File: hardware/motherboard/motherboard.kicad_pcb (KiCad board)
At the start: 4 copper layers, 152 x 68 mm, 82 parts, among them J1 IMU Connector, J2 JST-VH, J3 JST-VH, J4 JST-PH, J5 USB C 2.0, Q1 TSM7P06CP_ROG, Q2 TSM7P06CP_ROG, SW1 A, SW10 Right, SW11 Left, SW12 Up, SW13 Reset, SW2 B, SW3 X, SW4 Y, SW5 LB, SW6 RB, SW7 Start, SW8 Select, SW9 Down, U1 ESP32-S3-WROOM-1, U2 MCP73831-2-OT, U3 TPS75533KTTRG3, U4 TLV75709PDBV, U5 COM-09032

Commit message: Labelled Test Points
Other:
- board text added: "3V3"
- board text added: "Abat"
- board text added: "GND"
- board text added: "VBat"
- board text added: "VIN"
- board text added: "Vperipheral"
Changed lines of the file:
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@@
 		(layer "Edge.Cuts")
+	)
+	(gr_text "Vperipheral"
+		(at 80.01 40.64 0)
+		(layer "B.SilkS")
+		(effects
+			(font
+				(size 1 1)
+				(thickness 0.17)
+				(bold yes)
+			)
+			(justify left bottom mirror)
+		)
+	)
+	(gr_text "VBat"
+		(at 78.105 33.02 0)
+		(layer "B.SilkS")
+		(effects
+			(font
+				(size 1 1)
+				(thickness 0.17)
+				(bold yes)
+			)
+			(justify left bottom mirror)
+		)
+	)
+	(gr_text "3V3"
+		(at 103.505 28.575 0)
+		(layer "B.SilkS")
+		(effects
+			(font
+				(size 1 1)
+				(thickness 0.17)
+				(bold yes)
+			)
+			(justify left bottom mirror)
+		)
+	)
+	(gr_text "VIN"
+		(at 48.26 21.59 0)
+		(layer "B.SilkS")
+		(effects
+			(font
+				(size 1 1)
+				(thickness 0.17)
+				(bold yes)
+			)
+			(justify left bottom mirror)
+		)
+	)
+	(gr_text "GND"
+		(at 63.5 40.64 0)
+		(layer "B.SilkS")
+		(effects
+			(font
+				(size 1 1)
+				(thickness 0.17)
+				(bold yes)
+			)
+			(justify left bottom mirror)
+		)
+	)
+	(gr_text "Abat"
+		(at 82.55 33.02 0)
+		(layer "B.SilkS")
+		(effects
+			(font
+				(size 1 1)
+				(thickness 0.17)
+				(bold yes)
+			)
+			(justify left bottom mirror)
+		)
 	)
 	(gr_text "Battery"

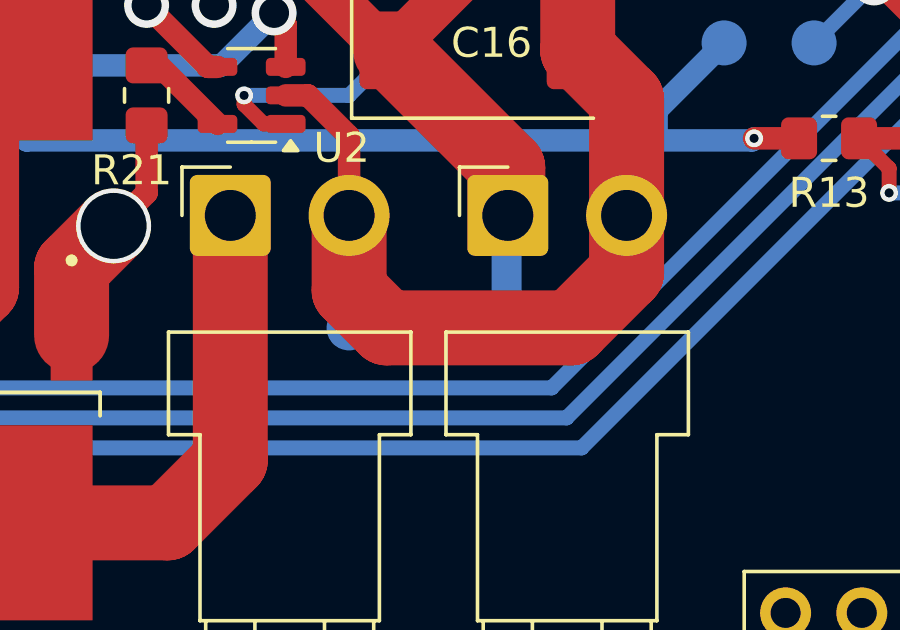
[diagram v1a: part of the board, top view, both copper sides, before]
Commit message: Labelled power connectors on Motherboard
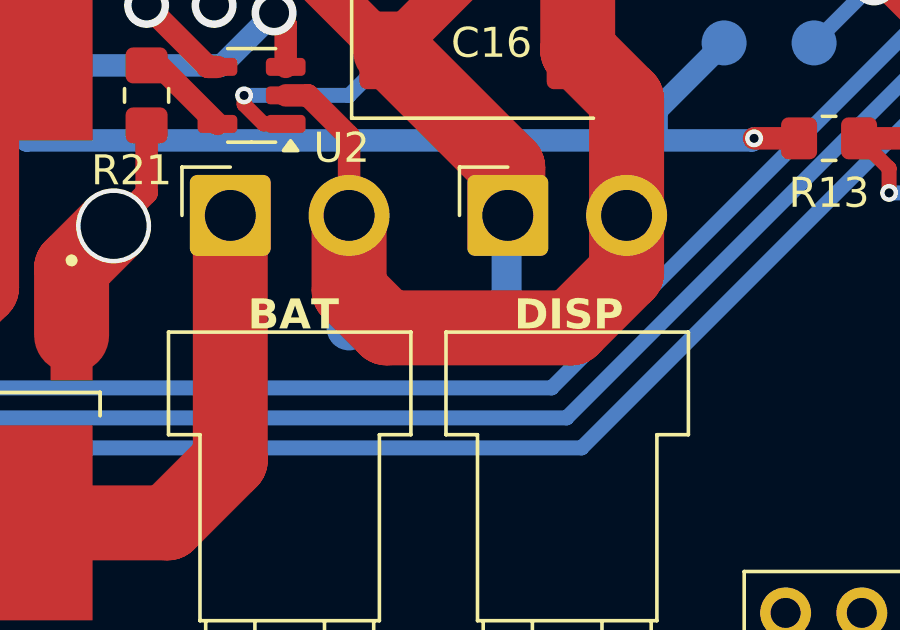
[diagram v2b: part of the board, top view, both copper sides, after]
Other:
- board text added: "BAT"
- board text added: "DISP"
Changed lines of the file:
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@@
 		(layer "Edge.Cuts")
+	)
+	(gr_text "BAT"
+		(at 61.372916 40.14 0)
+		(layer "F.SilkS")
+		(effects
+			(font
+				(size 1 1)
+				(thickness 0.17)
+				(bold yes)
+			)
+			(justify left bottom)
+		)
+	)
+	(gr_text "DISP"
+		(at 70.254377 40.14 0)
+		(layer "F.SilkS")
+		(effects
+			(font
+				(size 1 1)
+				(thickness 0.17)
+				(bold yes)
+			)
+			(justify left bottom)
+		)
 	)
 	(gr_text "Vperipheral"

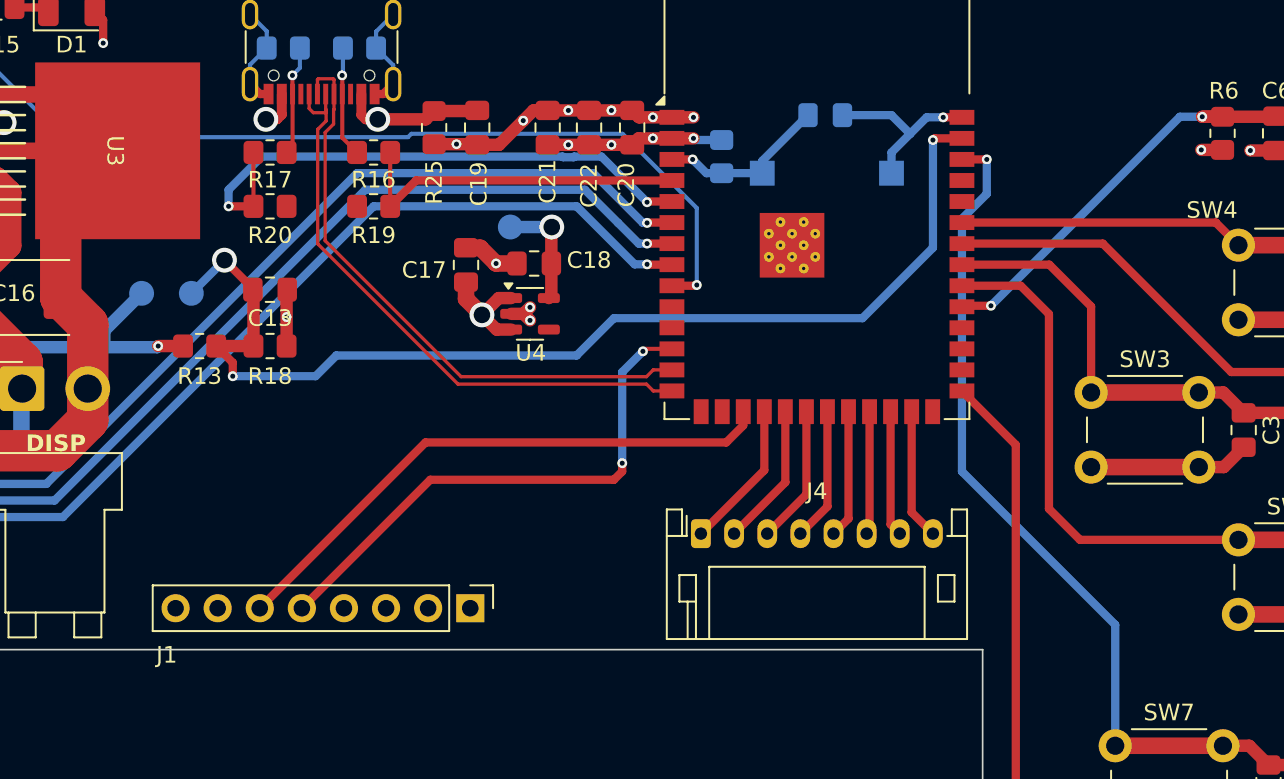
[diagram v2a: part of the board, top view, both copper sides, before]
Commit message: Updated Schematic, Added motor/speaker connector
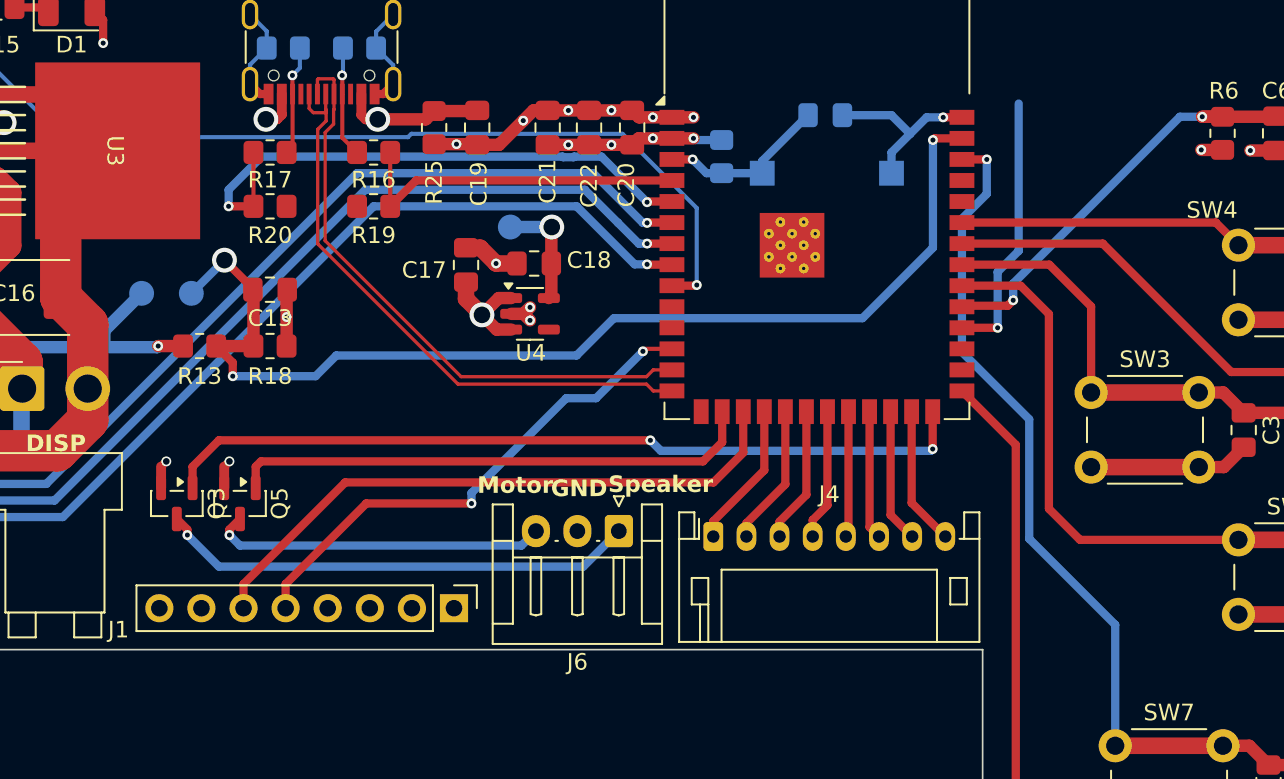
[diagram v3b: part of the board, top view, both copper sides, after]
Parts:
- added J6: Conn_01x03_Pin, Connector_JST:JST_EH_S3B-EH_1x03_P2.50mm_Horizontal, F.Cu at (106.0, 44.8)
- added Q3: AO3400A, Package_TO_SOT_SMD:SOT-23, F.Cu at (79.4, 43.2)
- added Q5: AO3400A, Package_TO_SOT_SMD:SOT-23, F.Cu at (83.2, 43.2)
- moved J1 0.98 mm to (87.6, 58.0)
- moved J4 0.77 mm to (111.7, 45.2)
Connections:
- U1 pad 16: unconnected-(U1-IO46-Pad16) -> Motor
- U1 pad 26: unconnected-(U1-IO45-Pad26) -> Speaker
- U1 pad 28: unconnected-(U1-IO35-Pad28) -> Left
- U1 pad 29: unconnected-(U1-IO36-Pad29) -> Down
- U1 pad 30: unconnected-(U1-IO37-Pad30) -> BLeft
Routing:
- net Speaker: track 0.00 -> 49.2 mm, vias 0 -> 2
- net Motor: track 0.00 -> 31.9 mm
- net Net-(J6-Pin_1): track 0.00 -> 28.9 mm, vias 0 -> 1
- net Net-(J6-Pin_3): track 0.00 -> 20.3 mm, vias 0 -> 1
- net VPeripheral: track 36.3 -> 55.3 mm, vias 0 -> 2
- net BLeft: track 7.76 -> 24.0 mm, vias 0 -> 1
- net SCL: track 34.6 -> 37.4 mm
- net SDA: track 32.3 -> 31.0 mm
- net BRight: track 28.7 -> 29.3 mm
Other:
- board text added: "Motor"
- board text added: "Speaker"

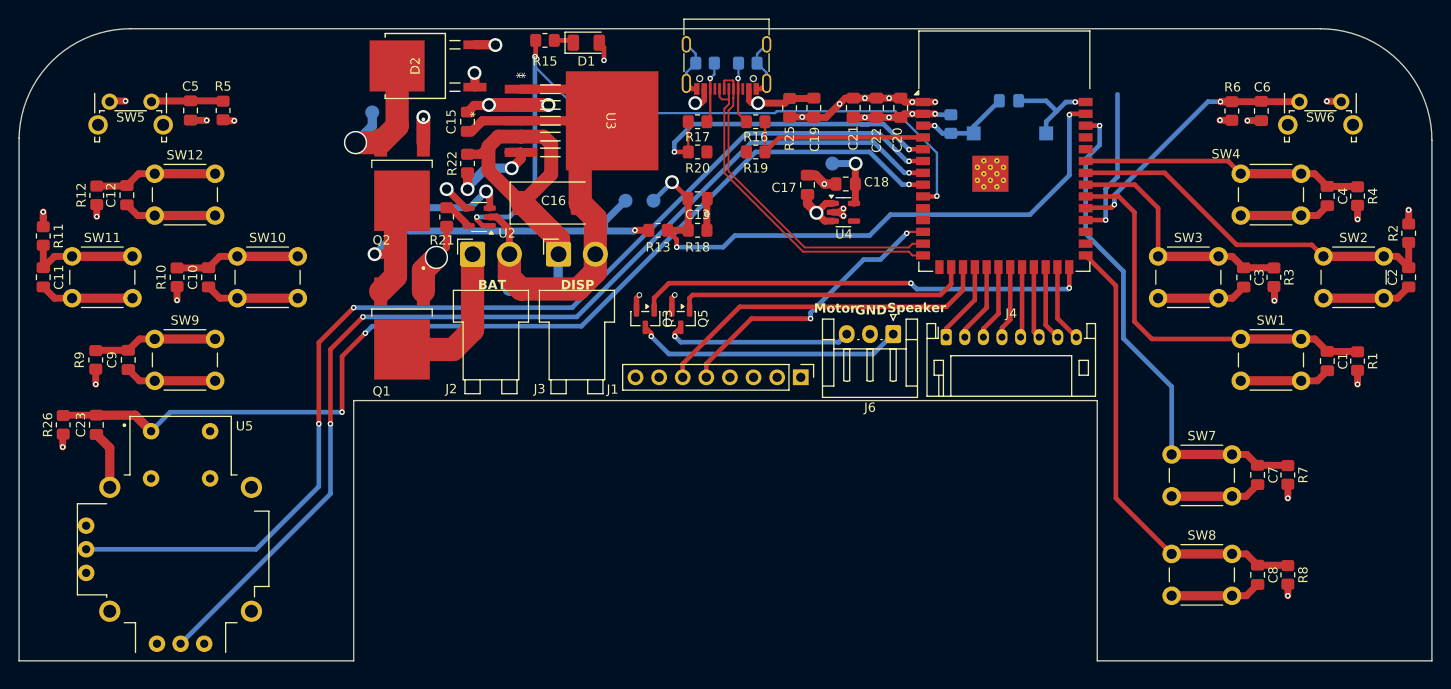
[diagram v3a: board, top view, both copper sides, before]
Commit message: Added ucbc 3d model
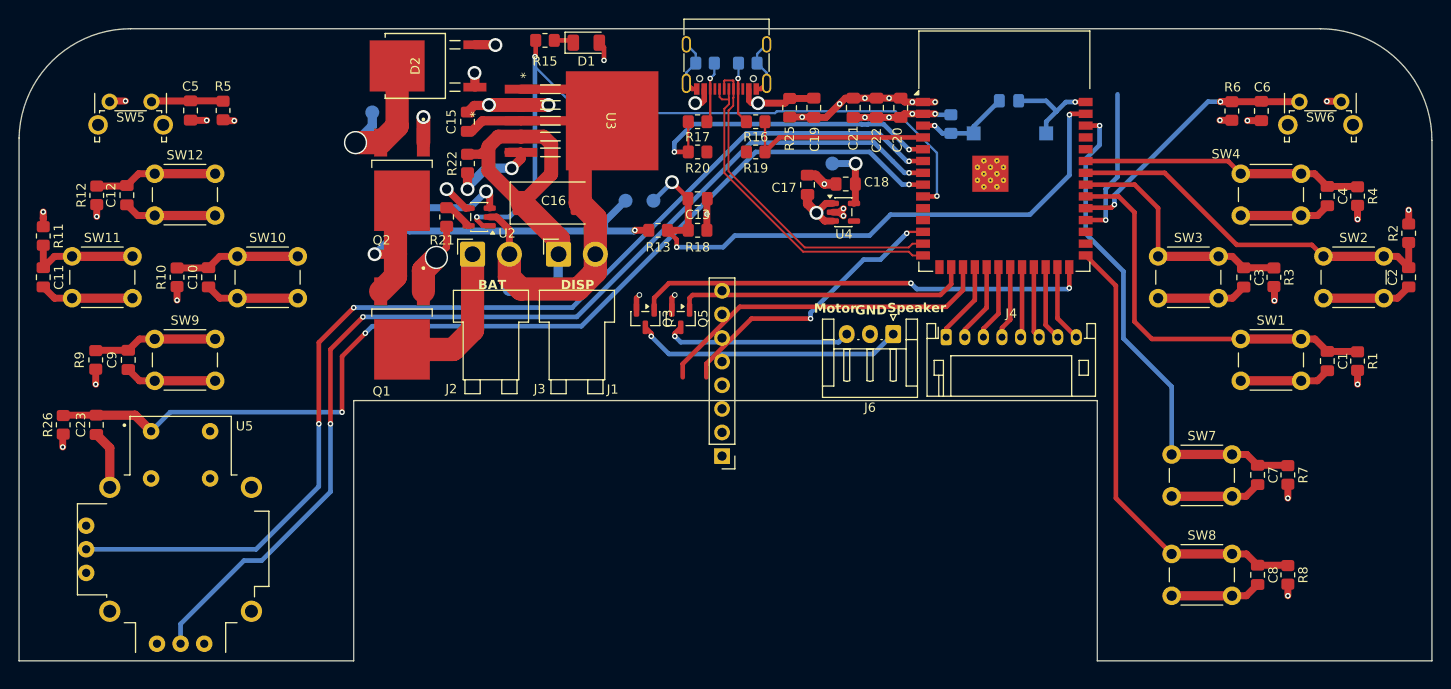
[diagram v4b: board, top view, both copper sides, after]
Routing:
- net AX: track 112.6 -> 113.8 mm
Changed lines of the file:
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@@
 			(pinfunction "Pin_2")
 			(pintype "passive")
-			(thermal_bridge_width 1)
 		)
 		(embedded_fonts no)
@@
 			(polygon
 				(pts
-					(xy 94 18.39) (xy 142.030402 18.474403) (xy 141.971359 -2.61) (xy 94 -2.61)
+					(xy 94 18.39) (xy 142 18.39) (xy 142 -2.61) (xy 94 -2.61)
 				)
 			)
@@
 		(attr smd)
 		(fp_line
-			(start 0 -1.56)
-			(end -0.8 -1.56)
+			(start -0.91 -1.56)
+			(end 0.91 -1.56)
 			(stroke
 				(width 0.12)
@@
 		)
 		(fp_line
-			(start 0 -1.56)
-			(end 0.8 -1.56)
+			(start -0.91 -1.51)
+			(end -0.91 -1.56)
 			(stroke
 				(width 0.12)
@@
 		)
 		(fp_line
-			(start 0 1.56)
-			(end -0.8 1.56)
+			(start -0.91 1.56)
+			(end -0.91 1.51)
 			(stroke
 				(width 0.12)
@@
 		)
 		(fp_line
-			(start 0 1.56)
-			(end 0.8 1.56)
+			(start 0.91 -1.56)
+			(end 0.91 -1.51)
+			(stroke
+				(width 0.12)
+				(type solid)
+			)
+			(layer "F.SilkS")
+		)
+		(fp_line
+			(start 0.91 -0.39)
+			(end 0.91 0.39)
+			(stroke
+				(width 0.12)
+				(type solid)
+			)
+			(layer "F.SilkS")
+		)
+		(fp_line
+			(start 0.91 1.51)
+			(end 0.91 1.56)
+			(stroke
+				(width 0.12)
+				(type solid)
+			)
+			(layer "F.SilkS")
+		)
+		(fp_line
+			(start 0.91 1.56)
+			(end -0.91 1.56)
 			(stroke
 				(width 0.12)
@@
 		(fp_poly
 			(pts
-				(xy -1.3 -1.51) (xy -1.54 -1.84) (xy -1.06 -1.84)
+				(xy -1.45 -1.51) (xy -1.69 -1.84) (xy -1.21 -1.84)
 			)
 			(stroke
@@
 		)
 		(embedded_fonts no)
-		(model "${KICAD9_3DMODEL_DIR}/Connector_USB.3dshapes/USB_C_Receptacle_G-Switch_GT-USB-7010ASV.step"
+		(model "${OPS2_HANDHELD}/esp_32_handheld.3dshapes/664_12402012E212A.stp"
 			(offset
-				(xyz 0 0 0)
+				(xyz 40 1 1.5)
 			)
 			(scale
@@
 			)
 			(rotate
-				(xyz 0 0 0)
+				(xyz -90 -0 -0)
 			)
 		)
@@
 		)
 		(fp_text user "*"
-			(at -4.884999 9.652 90)
+			(at -4.884999 9.652 270)
+			(unlocked yes)
 			(layer "F.SilkS")
 			(effects
@@
 		)
 		(fp_text user "*"
-			(at -4.884999 9.652 90)
+			(at -4.884999 9.652 270)
+			(unlocked yes)
 			(layer "F.Fab")
 			(effects
@@
 			(pinfunction "Pin_2")
 			(pintype "passive")
-			(thermal_bridge_width 1)
 		)
 		(embedded_fonts no)
@@
 		(fp_text user "*"
 			(at -5.195001 6.4135 90)
-			(unlocked yes)
 			(layer "F.SilkS")
 			(effects
@@
 		(attr smd)
 		(fp_line
-			(start 0 1.56)
-			(end 0.8 1.56)
+			(start 0.91 1.56)
+			(end -0.91 1.56)
+			(stroke
+				(width 0.12)
+				(type solid)
+			)
+			(layer "F.SilkS")
+		)
+		(fp_line
+			(start 0.91 1.51)
+			(end 0.91 1.56)
+			(stroke
+				(width 0.12)
+				(type solid)
+			)
+			(layer "F.SilkS")
+		)
+		(fp_line
+			(start 0.91 -0.39)
+			(end 0.91 0.39)
+			(stroke
+				(width 0.12)
+				(type solid)
+			)
+			(layer "F.SilkS")
+		)
+		(fp_line
+			(start 0.91 -1.56)
+			(end 0.91 -1.51)
 			(stroke
 				(width 0.12)
@@
 		)
 		(fp_line
-			(start 0 1.56)
-			(end -0.8 1.56)
+			(start -0.91 1.56)
+			(end -0.91 1.51)
 			(stroke
 				(width 0.12)
@@
 		)
 		(fp_line
-			(start 0 -1.56)
-			(end 0.8 -1.56)
+			(start -0.91 -1.51)
+			(end -0.91 -1.56)
 			(stroke
 				(width 0.12)
@@
 		)
 		(fp_line
-			(start 0 -1.56)
-			(end -0.8 -1.56)
+			(start -0.91 -1.56)
+			(end 0.91 -1.56)
 			(stroke
 				(width 0.12)
@@
 		(fp_poly
 			(pts
-				(xy -1.3 -1.51) (xy -1.54 -1.84) (xy -1.06 -1.84)
+				(xy -1.45 -1.51) (xy -1.69 -1.84) (xy -1.21 -1.84)
 			)
 			(stroke
@@
 		(attr through_hole)
 		(fp_line
-			(start 10.69 9.85)
-			(end 10.69 7.09)
+			(start 1.38 1.27)
+			(end 1.38 19.16)
 			(stroke
 				(width 0.12)
@@
 		)
 		(fp_line
-			(start -7.2 9.85)
-			(end 10.69 9.85)
+			(start -1.38 19.16)
+			(end 1.38 19.16)
 			(stroke
 				(width 0.12)
@@
 		)
 		(fp_line
-			(start -7.2 9.85)
-			(end -7.2 7.09)
+			(start -1.38 1.27)
+			(end 1.38 1.27)
 			(stroke
 				(width 0.12)
@@
 		)
 		(fp_line
-			(start -7.2 7.09)
-			(end 10.69 7.09)
+			(start -1.38 1.27)
+			(end -1.38 19.16)
 			(stroke
 				(width 0.12)
@@
 		)
 		(fp_line
-			(start -8.47 9.85)
-			(end -9.85 9.85)
+			(start -1.38 0)
+			(end -1.38 -1.38)
 			(stroke
 				(width 0.12)
@@
 		)
 		(fp_line
-			(start -9.85 9.85)
-			(end -9.85 8.47)
+			(start -1.38 -1.38)
+			(end 0 -1.38)
 			(stroke
 				(width 0.12)
@@
 		)
 		(fp_line
-			(start 11.08 10.24)
-			(end 11.08 6.7)
+			(start 1.77 19.55)
+			(end 1.77 -1.77)
 			(stroke
 				(width 0.05)
@@
 		)
 		(fp_line
-			(start 11.08 6.7)
-			(end -10.24 6.7)
+			(start 1.77 -1.77)
+			(end -1.77 -1.77)
 			(stroke
 				(width 0.05)
@@
 		)
 		(fp_line
-			(start -10.24 10.24)
-			(end 11.08 10.24)
+			(start -1.77 19.55)
+			(end 1.77 19.55)
 			(stroke
 				(width 0.05)
@@
 		)
 		(fp_line
-			(start -10.24 6.7)
-			(end -10.24 10.24)
+			(start -1.77 -1.77)
+			(end -1.77 19.55)
 			(stroke
 				(width 0.05)
@@
 			(layer "F.CrtYd")
 		)
-		(fp_rect
-			(start -10.2 6.7)
-			(end 11.1 21.3)
-			(stroke
-				(width 0.1)
-				(type solid)
-			)
-			(fill no)
-			(layer "F.CrtYd")
-		)
 		(fp_line
-			(start 10.58 9.74)
-			(end -9.105 9.74)
+			(start 1.27 19.05)
+			(end -1.27 19.05)
 			(stroke
 				(width 0.1)
@@
 		)
 		(fp_line
-			(start 10.58 7.2)
-			(end 10.58 9.74)
+			(start 1.27 -1.27)
+			(end 1.27 19.05)
 			(stroke
 				(width 0.1)
@@
 		)
 		(fp_line
-			(start -9.105 9.74)
-			(end -9.74 9.105)
+			(start -0.635 -1.27)
+			(end 1.27 -1.27)
 			(stroke
 				(width 0.1)
@@
 		)
 		(fp_line
-			(start -9.74 9.105)
-			(end -9.74 7.2)
+			(start -1.27 19.05)
+			(end -1.27 -0.635)
 			(stroke
 				(width 0.1)
@@
 		)
 		(fp_line
-			(start -9.74 7.2)
-			(end 10.58 7.2)
+			(start -1.27 -0.635)
+			(end -0.635 -1.27)
 			(stroke
 				(width 0.1)
@@
 		)
 		(pad "1" thru_hole rect
-			(at -8.47 8.47 270)
+			(at 0 0 180)
 			(size 1.7 1.7)
 			(drill 1)
@@
 		)
 		(pad "2" thru_hole circle
-			(at -5.93 8.47 270)
+			(at 0 2.54 180)
 			(size 1.7 1.7)
 			(drill 1)
@@
 		)
 		(pad "3" thru_hole circle
-			(at -3.39 8.47 270)
+			(at 0 5.08 180)
 			(size 1.7 1.7)
 			(drill 1)
@@
 		)
 		(pad "4" thru_hole circle
-			(at -0.85 8.47 270)
+			(at 0 7.62 180)
 			(size 1.7 1.7)
 			(drill 1)
@@
 		)
 		(pad "5" thru_hole circle
-			(at 1.69 8.47 270)
+			(at 0 10.16 180)
 			(size 1.7 1.7)
 			(drill 1)
@@
 		)
 		(pad "6" thru_hole circle
-			(at 4.23 8.47 270)
+			(at 0 12.7 180)
 			(size 1.7 1.7)
 			(drill 1)
@@
 		)
 		(pad "7" thru_hole circle
-			(at 6.77 8.47 270)
+			(at 0 15.24 180)
 			(size 1.7 1.7)
 			(drill 1)
@@
 		)
 		(pad "8" thru_hole circle
-			(at 9.31 8.47 270)
+			(at 0 17.78 180)
 			(size 1.7 1.7)
 			(drill 1)
@@
 		)
 		(embedded_fonts no)
-		(model "${OPS2_HANDHELD}/esp_32_handheld.3dshapes/MPU 6050 IMU.STEP"
+		(model "${KICAD9_3DMODEL_DIR}/Connector_PinHeader_2.54mm.3dshapes/PinHeader_1x08_P2.54mm_Vertical.step"
 			(offset
-				(xyz -6.75 1.4 -8)
+				(xyz 0 0 0)
 			)
 			(scale
@@
 			)
 			(rotate
-				(xyz -90 -0 -0)
+				(xyz 0 0 0)
 			)
 		)
@@
 	)
 	(segment
+		(start 45.5 61.815)
+		(end 38.1 69.215)
+		(width 0.5)
+		(layer "B.Cu")
+		(net 42)
+	)
+	(segment
 		(start 107.75 27.5)
 		(end 107.25 27.5)
@@
 	)
 	(segment
-		(start 45.5 54.5)
-		(end 45.5 62.04)
+		(start 38.1 69.215)
+		(end 36.195 69.215)
 		(width 0.5)
 		(layer "B.Cu")
@@
 	)
 	(segment
-		(start 45.5 62.04)
+		(start 45.5 54.5)
+		(end 45.5 61.815)
+		(width 0.5)
+		(layer "B.Cu")
+		(net 42)
+	)
+	(segment
+		(start 36.195 69.215)
+		(end 29.38 76.03)
+		(width 0.5)
+		(layer "B.Cu")
+		(net 42)
+	)
+	(segment
+		(start 29.38 76.03)
 		(end 29.38 78.16)
 		(width 0.5)
